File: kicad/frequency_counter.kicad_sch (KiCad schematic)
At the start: 27 parts, among them J101 SMA, J102 SMA, J102 USB-C, J103 DISPLAY, SW1 SW_SPST, SW103 SPST, SW2 SW_SPST

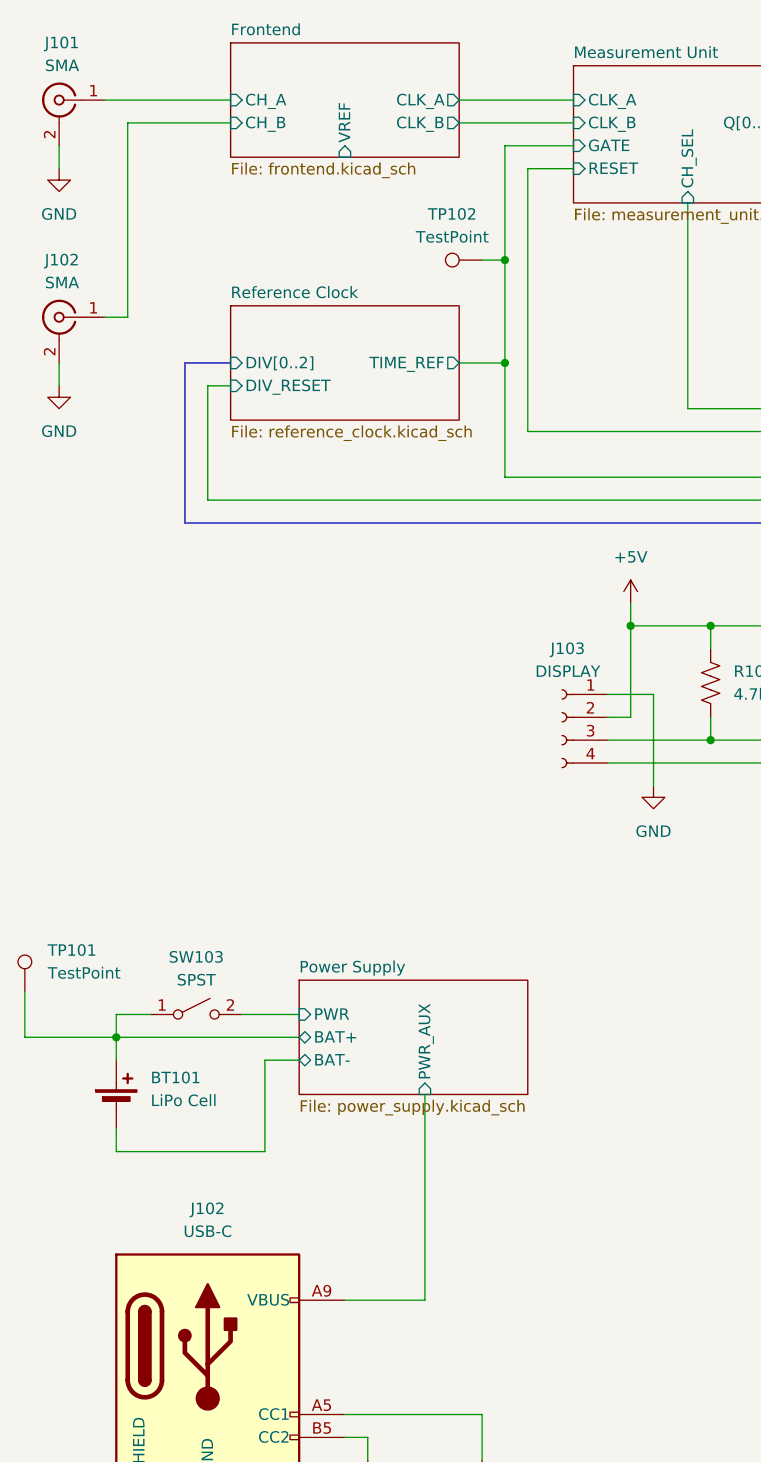
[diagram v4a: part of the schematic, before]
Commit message: ch a voltage reference, ch b hysteresis
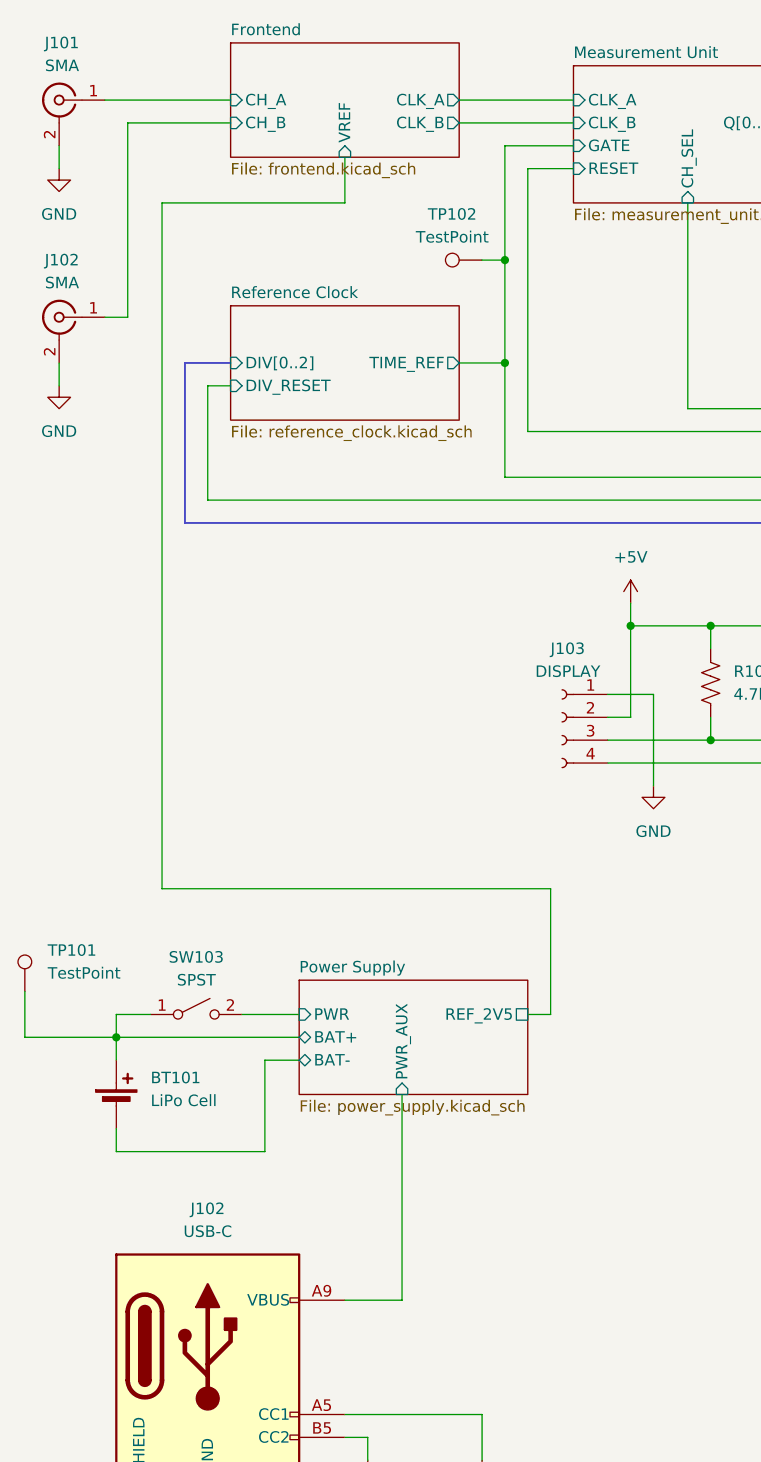
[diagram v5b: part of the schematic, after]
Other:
- sheet Power Supply ports: added REF_2V5; removed none
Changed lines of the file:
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@@
 	(wire
 		(pts
+			(xy 74.93 129.54) (xy 74.93 115.57)
+		)
+		(stroke
+			(width 0)
+			(type default)
+		)
+	)
+	(wire
+		(pts
 			(xy 171.45 33.02) (xy 140.97 33.02)
 		)
@@
 	(wire
 		(pts
+			(xy 74.93 115.57) (xy 31.75 115.57)
+		)
+		(stroke
+			(width 0)
+			(type default)
+		)
+	)
+	(wire
+		(pts
 			(xy 215.9 46.99) (xy 215.9 49.53)
 		)
@@
 	(wire
 		(pts
+			(xy 31.75 39.37) (xy 52.07 39.37)
+		)
+		(stroke
+			(width 0)
+			(type default)
+		)
+	)
+	(wire
+		(pts
 			(xy 16.51 132.08) (xy 16.51 127)
 		)
@@
 	(wire
 		(pts
+			(xy 52.07 39.37) (xy 52.07 34.29)
+		)
+		(stroke
+			(width 0)
+			(type default)
+		)
+	)
+	(wire
+		(pts
 			(xy 228.6 26.67) (xy 228.6 29.21)
 		)
@@
 	(wire
 		(pts
-			(xy 52.07 161.29) (xy 60.96 161.29)
+			(xy 52.07 161.29) (xy 58.42 161.29)
 		)
 		(stroke
@@
 	(wire
 		(pts
+			(xy 31.75 115.57) (xy 31.75 39.37)
+		)
+		(stroke
+			(width 0)
+			(type default)
+		)
+	)
+	(wire
+		(pts
 			(xy 104.14 96.52) (xy 104.14 101.6)
 		)
@@
 	(wire
 		(pts
+			(xy 72.39 129.54) (xy 74.93 129.54)
+		)
+		(stroke
+			(width 0)
+			(type default)
+		)
+	)
+	(wire
+		(pts
 			(xy 120.65 62.23) (xy 90.17 62.23)
 		)
@@
 	(wire
 		(pts
-			(xy 60.96 161.29) (xy 60.96 138.43)
+			(xy 58.42 161.29) (xy 58.42 138.43)
 		)
 		(stroke
@@
 		)
 		(pin "PWR_AUX" input
-			(at 60.96 138.43 270)
+			(at 58.42 138.43 270)
 			(effects
 				(font
@@
 			)
 		)
+		(pin "REF_2V5" passive
+			(at 72.39 129.54 0)
+			(effects
+				(font
+					(size 1.27 1.27)
+				)
+				(justify right)
+			)
+		)

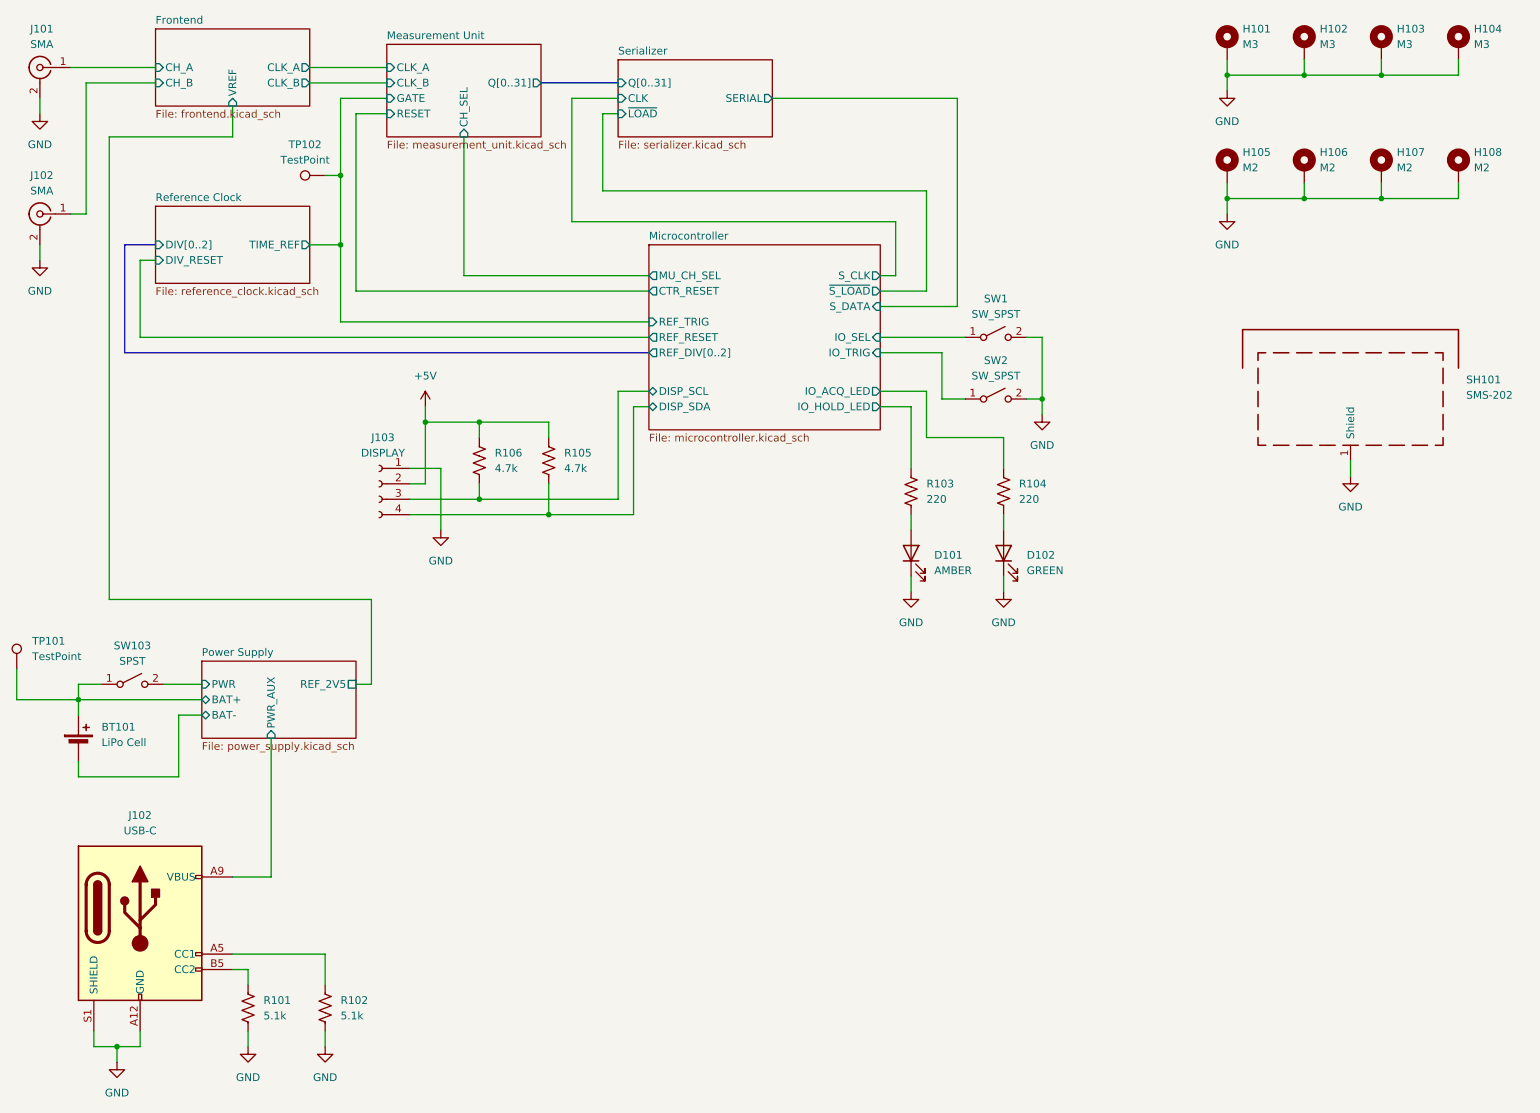
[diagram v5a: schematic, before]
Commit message: rework frontend, channel gating
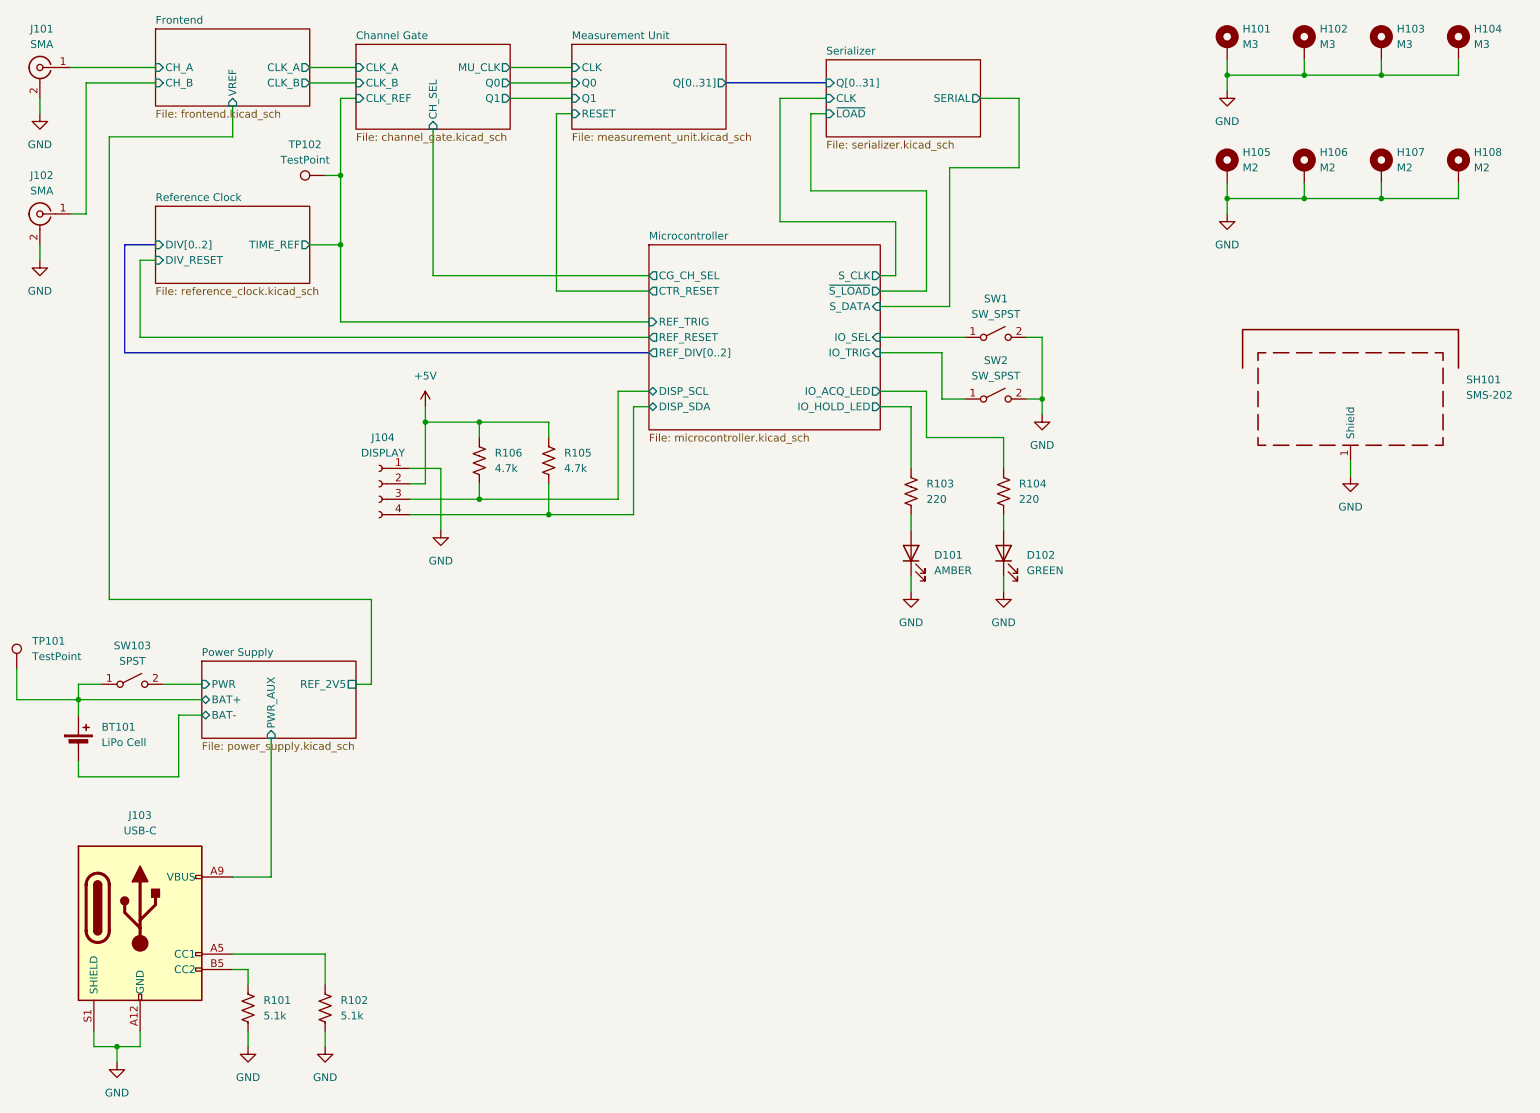
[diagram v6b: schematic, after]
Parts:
- renumbered J102 to J103, J103 to J104
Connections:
- net Measurement Unit/GATE renamed Channel Gate/CLK_REF
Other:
- added sheet Channel Gate (channel_gate.kicad_sch)
- sheet Measurement Unit ports: added CLK, Q0, Q1; removed CH_SEL, CLK_A, CLK_B, GATE
- sheet Microcontroller ports: added CG_CH_SEL; removed MU_CH_SEL

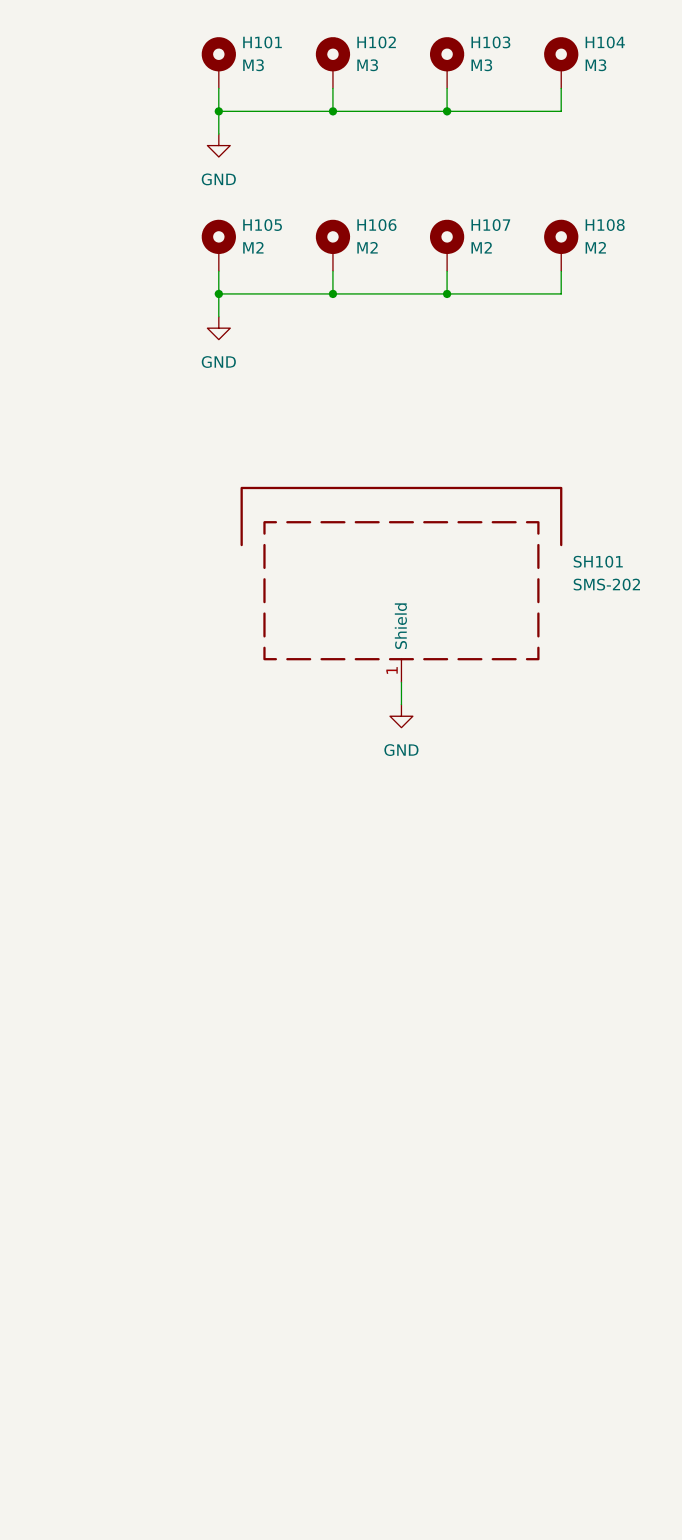
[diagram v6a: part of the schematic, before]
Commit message: replace alum caps with ceramics, change mpn labeling
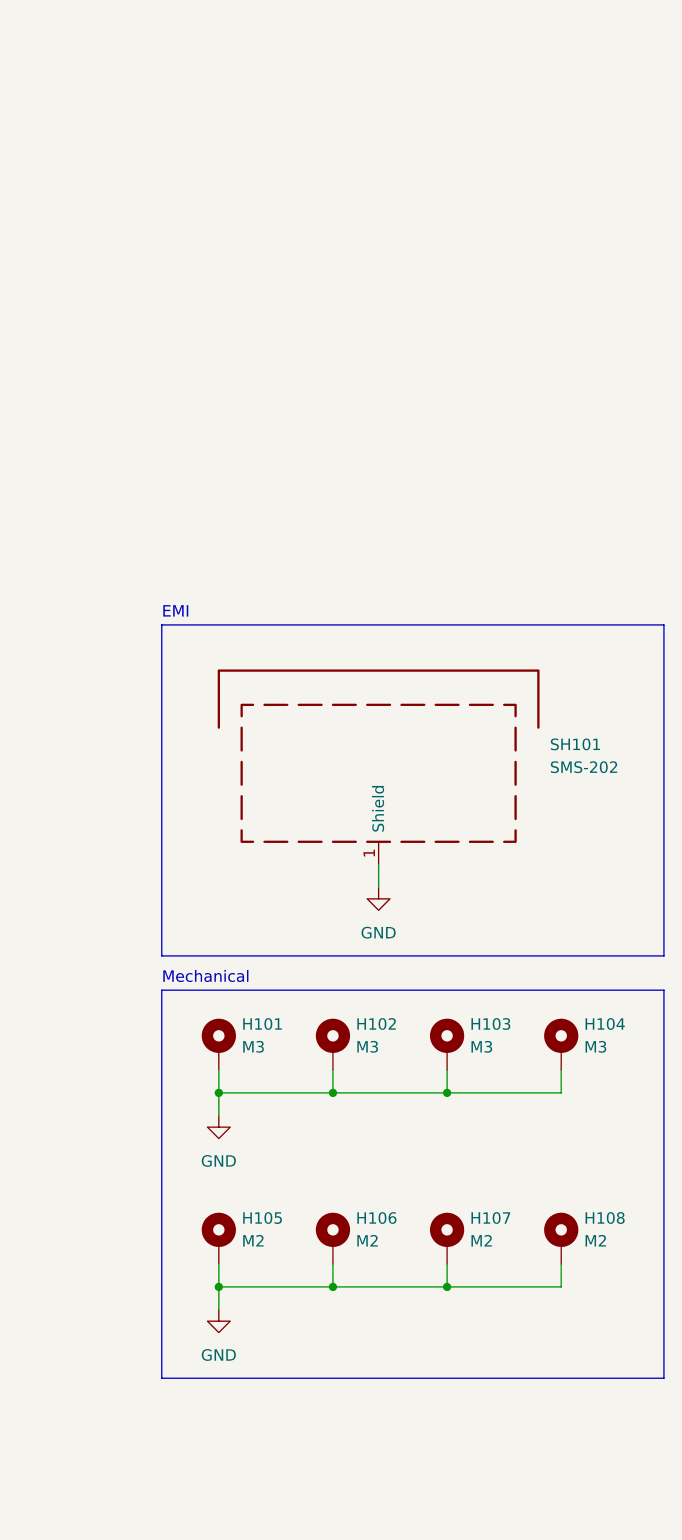
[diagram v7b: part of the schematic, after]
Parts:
- D101: MPN (none) -> B1911UY--20D000114U1930; Supplier https://www.digikey.com/en/products/detail/harvatek-corpora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 -> (none)
- D102: MPN (none) -> B1911NG--20D000214U1930; Supplier https://www.digikey.com/en/products/detail/harvatek-corpora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 -> (none)
- J101, J102: MPN (none) -> CON-SMA-EDGE-S; Supplier https://www.digikey.com/en/products/detail/rf-solutions/CON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 -> (none)
- J103: MPN (none) -> USB4125-GF-A; Supplier https://www.digikey.com/en/products/detail/gct/USB4125-GF-A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 -> (none)
- J104: Supplier Generic -> (none)
- R101, R102: MPN (none) -> RC0402JR-135K1L; Supplier https://www.digikey.com/en/products/detail/yageo/RC0402JR-1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 -> (none)
- R103, R104: MPN (none) -> RC0402JR-13220RL; Supplier https://www.digikey.com/en/products/detail/yageo/RC0402JR-1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 -> (none)
- SH101: MPN (none) -> SMS-201F; Supplier https://www.digikey.com/en/products/detail/leader-tech-inc/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 -> (none)
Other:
- note added: "EMI"
- note added: "Mechanical"
- moved on the sheet: H101, H102, H103, H104, H105, H106, H107, H108, SH101
